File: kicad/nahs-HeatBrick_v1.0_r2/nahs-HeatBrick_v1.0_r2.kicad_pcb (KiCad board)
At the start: 2 copper layers, 45 x 70 mm, 62 parts, among them IC1 ESP12S, IC2 ATTINY414, J2 AKL 101-02, J3 AKL 101-02, Q1 BSS138, Q3 BS170, SW1 KMR_231_G_LFS, SW2 SSSS820101, SW3 SW_DIP_x04, SW4 Taster_3301, SW5 Taster_4545, U1 MCP1700-3302, U2 LM1086_IT5,0

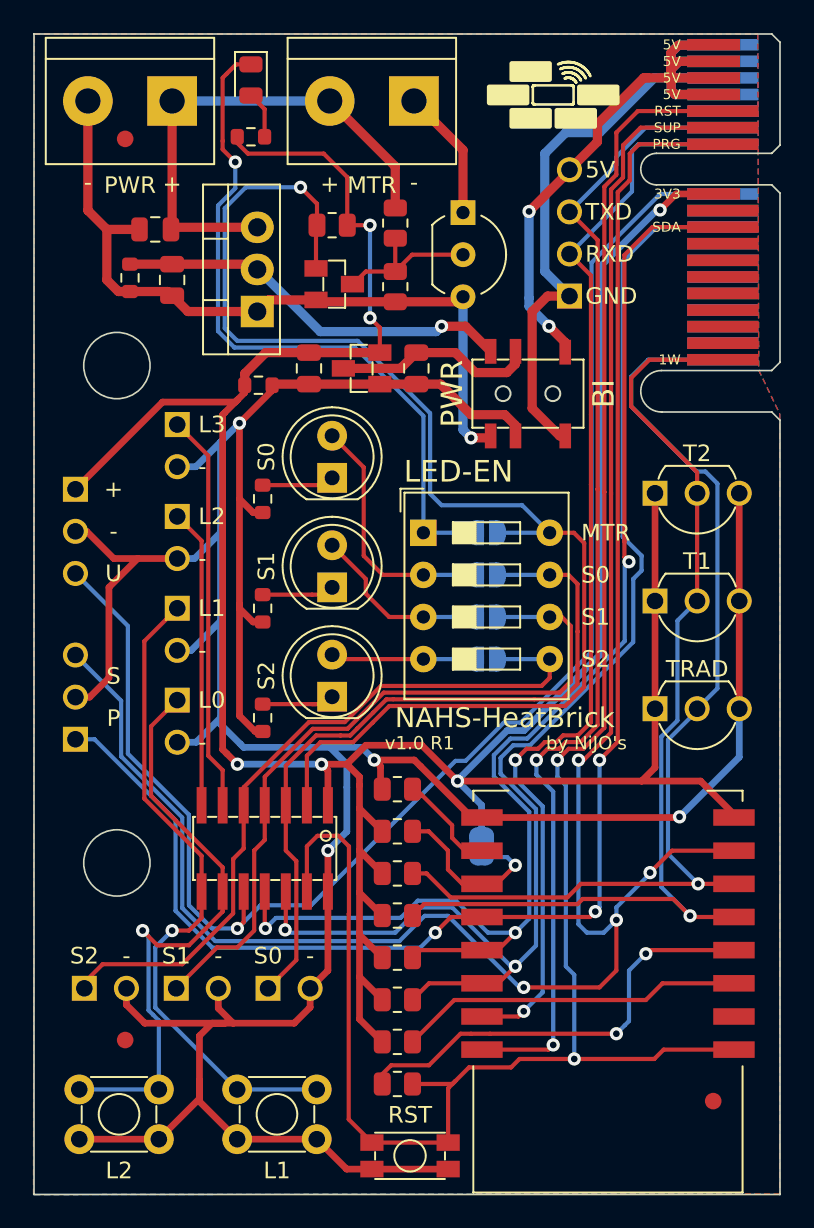
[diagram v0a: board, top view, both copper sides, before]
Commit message: v1.0 R2 Board updated DS18B20 Footprint
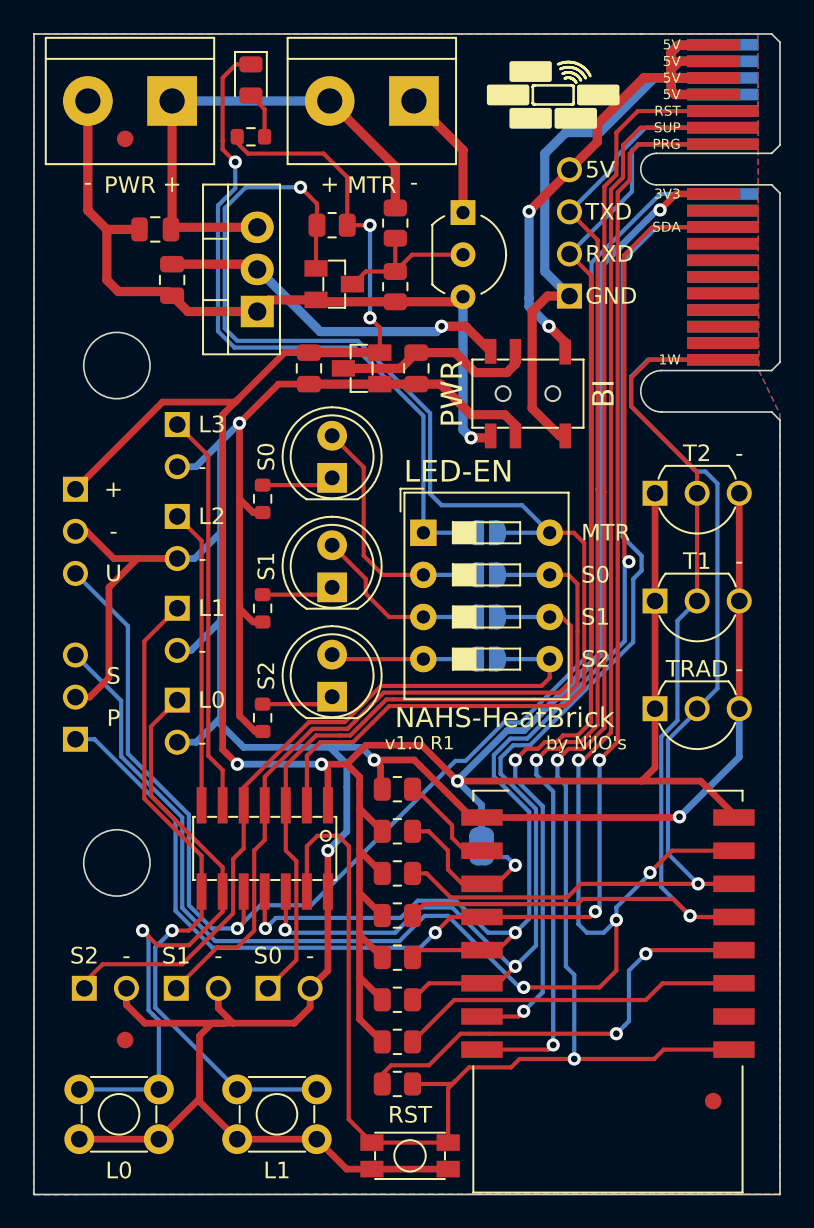
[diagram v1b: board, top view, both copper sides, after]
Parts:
- removed R20: 510, no_common:R_0603_1608Metric
- removed R21: 330, no_common:R_0603_1608Metric
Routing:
- net Net-(C4-Pad1): track 24.2 -> 21.7 mm
- net +3V3: track 193.0 -> 192.3 mm

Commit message: v1.0 R2 Board done
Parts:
- U2: value LM1086_IT5,0 -> PXO7805-500-S; footprint Package_TO_SOT_THT:TO-220-3_Vertical -> no_common:PXO7805-500-S
- moved C1 3.22 mm to (110.5, 82.3), turned to -90 degrees
- moved C1 2.50 mm to (110.5, 86.1), turned to 90 degrees
- moved U2 2.42 mm to (113.3, 84.3), turned to -90 degrees
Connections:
- U2 pad 1: 24- -> 24+
- U2 pad 2: Net-(C4-Pad1) -> 24-
- U2 pad 3: 24+ -> Net-(C4-Pad1)
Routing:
- net Net-(C4-Pad1): track 21.7 -> 18.3 mm
- net 24-: track 45.9 -> 43.5 mm
- net 24+: track 30.6 -> 28.8 mm
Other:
- board text added: "MTR"
- board text added: "PWR"
- board text added: "v1.0 R2"
- board text removed: "v1.0 R1"
